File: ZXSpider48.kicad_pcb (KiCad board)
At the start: 2 copper layers, 213.5 x 130.5 mm, 152 parts, among them J1 Barrel_Jack_Switch, J11 EAR/MIC, J12 KB_CONN_05, J14 RESET, J15 ZX_48K_EDGE, J16 DB9_Pins, J17 ON/OFF, J18 JS_ENABLE, J19 AY3_IOB, J2 JTAG, J20 AY3_IOA, J3 9V, J4 AUDIO, J5 ROM_SW, J6 M-DIN KMDGX-9S-BS-1, J7 SPK_ON_OFF, J8 KB_CON_08, J9 UV/EEPROM, Q1 BC517, Q10 BC560, Q11 BC560, Q12 BC560, Q13 BC560, Q14 BC560, Q15 BC560, Q2 BC548, Q8 BC560, Q9 BC560, U1 AY-3-8912, U10 27/28C256, U11 74HCT240, U16 74LS138, U18 74LS00, U2 EPM7128SLC84-10, U3 LM7805_TO220, U4 AY-3-8910, U5 HM62256, U6 74HC04, U7 HM62256, U8 Z80, U9 74LS32, Y2 14.000 Mhz

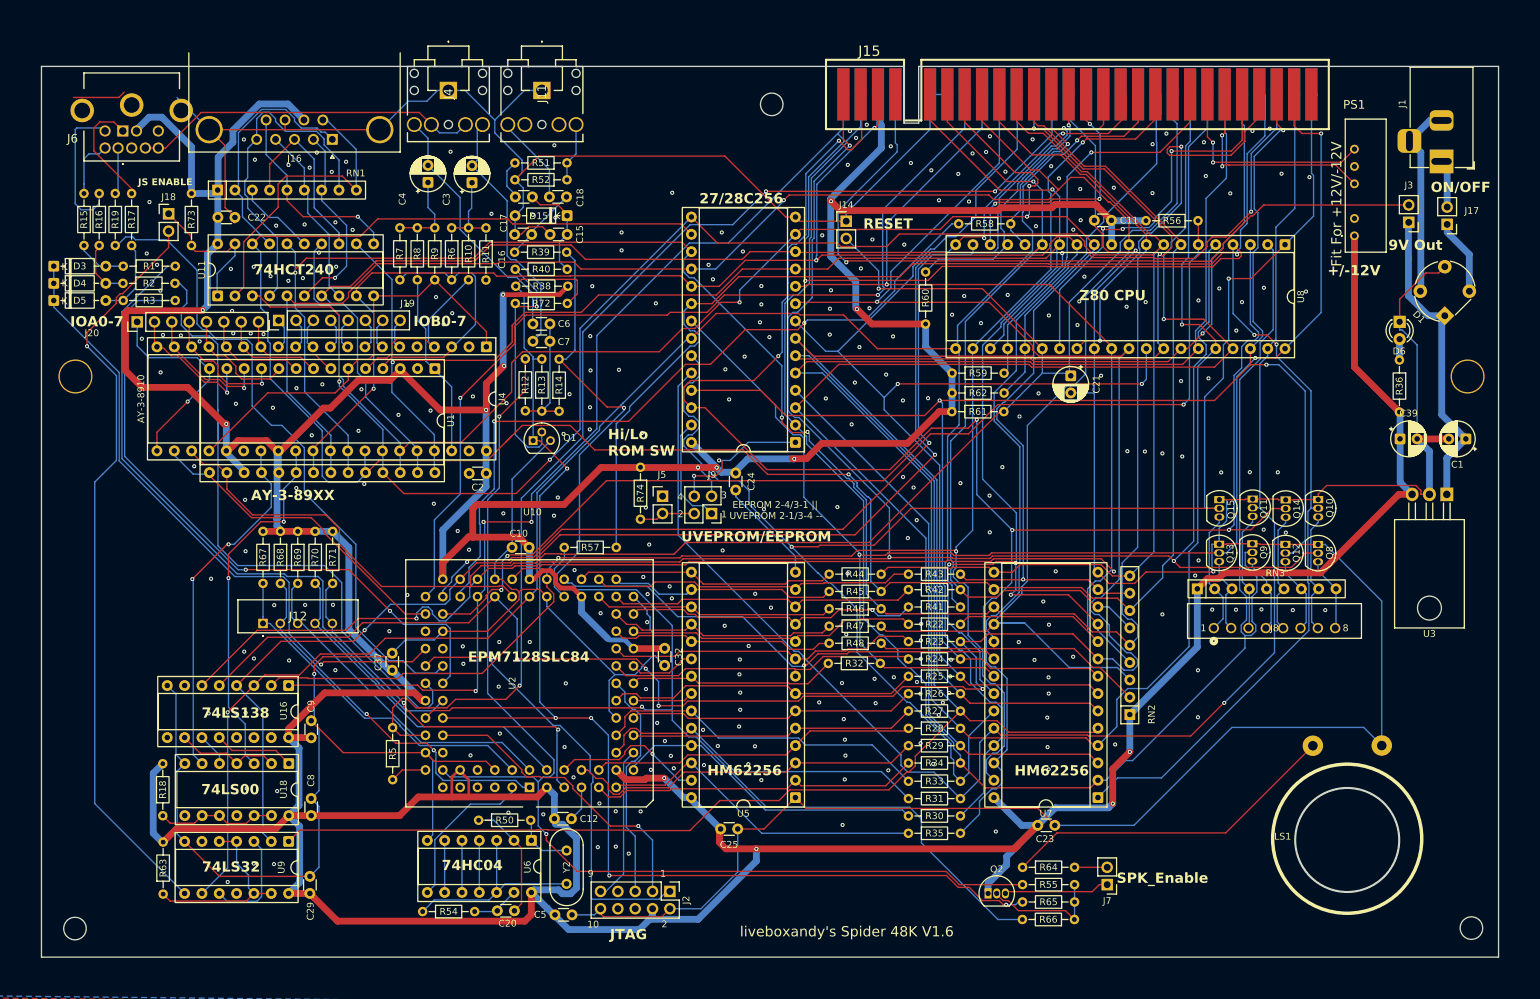
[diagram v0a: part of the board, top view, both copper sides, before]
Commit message: Add files via upload
Minor change to reduce PCB size to better fit some Rubber cases.
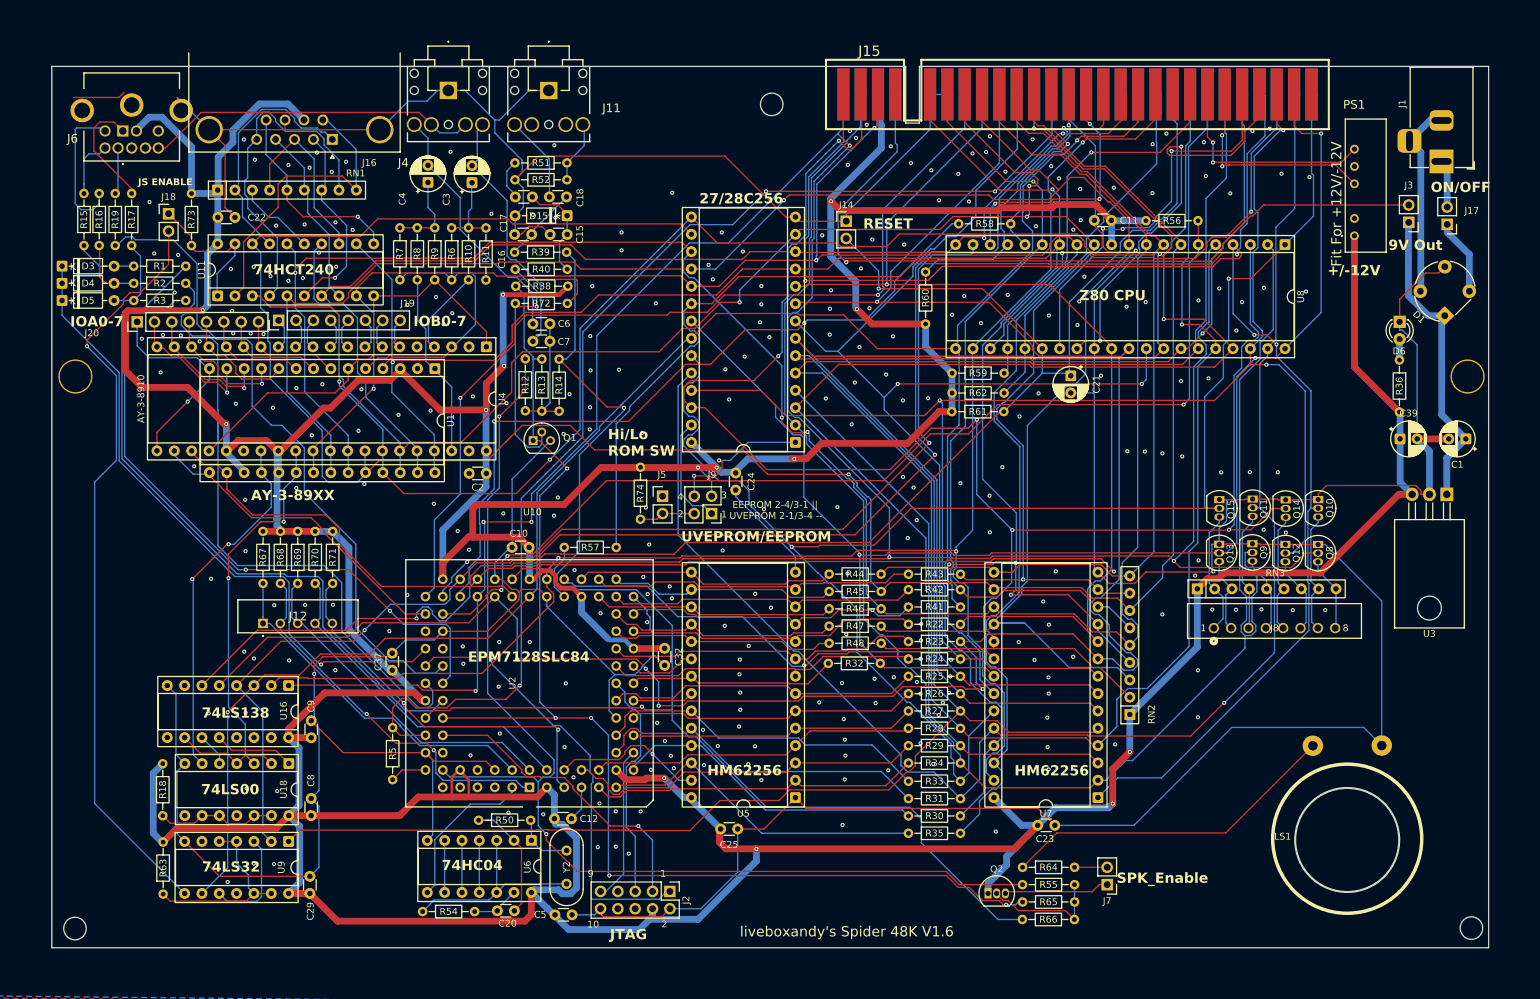
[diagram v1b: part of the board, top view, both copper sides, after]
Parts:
- moved R2 1.58 mm to (37.5, 53.7)
- moved R3 1.55 mm to (37.5, 56.2)
- moved R1 1.54 mm to (37.5, 51.1)
- moved D3 1.22 mm to (27.0, 51.1)
- moved D4 1.22 mm to (27.0, 53.7)
- moved D5 1.22 mm to (27.0, 56.2)
- moved J11 1.00 mm to (98.3, 25.4)
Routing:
- net GND: track 889.2 -> 890.7 mm
- net Net-(D3-A): track 7.36 -> 8.70 mm
- net RED: track 99.0 -> 100.3 mm
- net BLUE: track 95.7 -> 96.9 mm
- net Net-(J18-Pin_2): track 110.8 -> 111.4 mm
- net Net-(J11-Tip): track 13.1 -> 13.7 mm
- net CSYNC: track 96.4 -> 97.0 mm
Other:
- board size 213.5 x 130.5 mm -> 210.5 x 129.1 mm

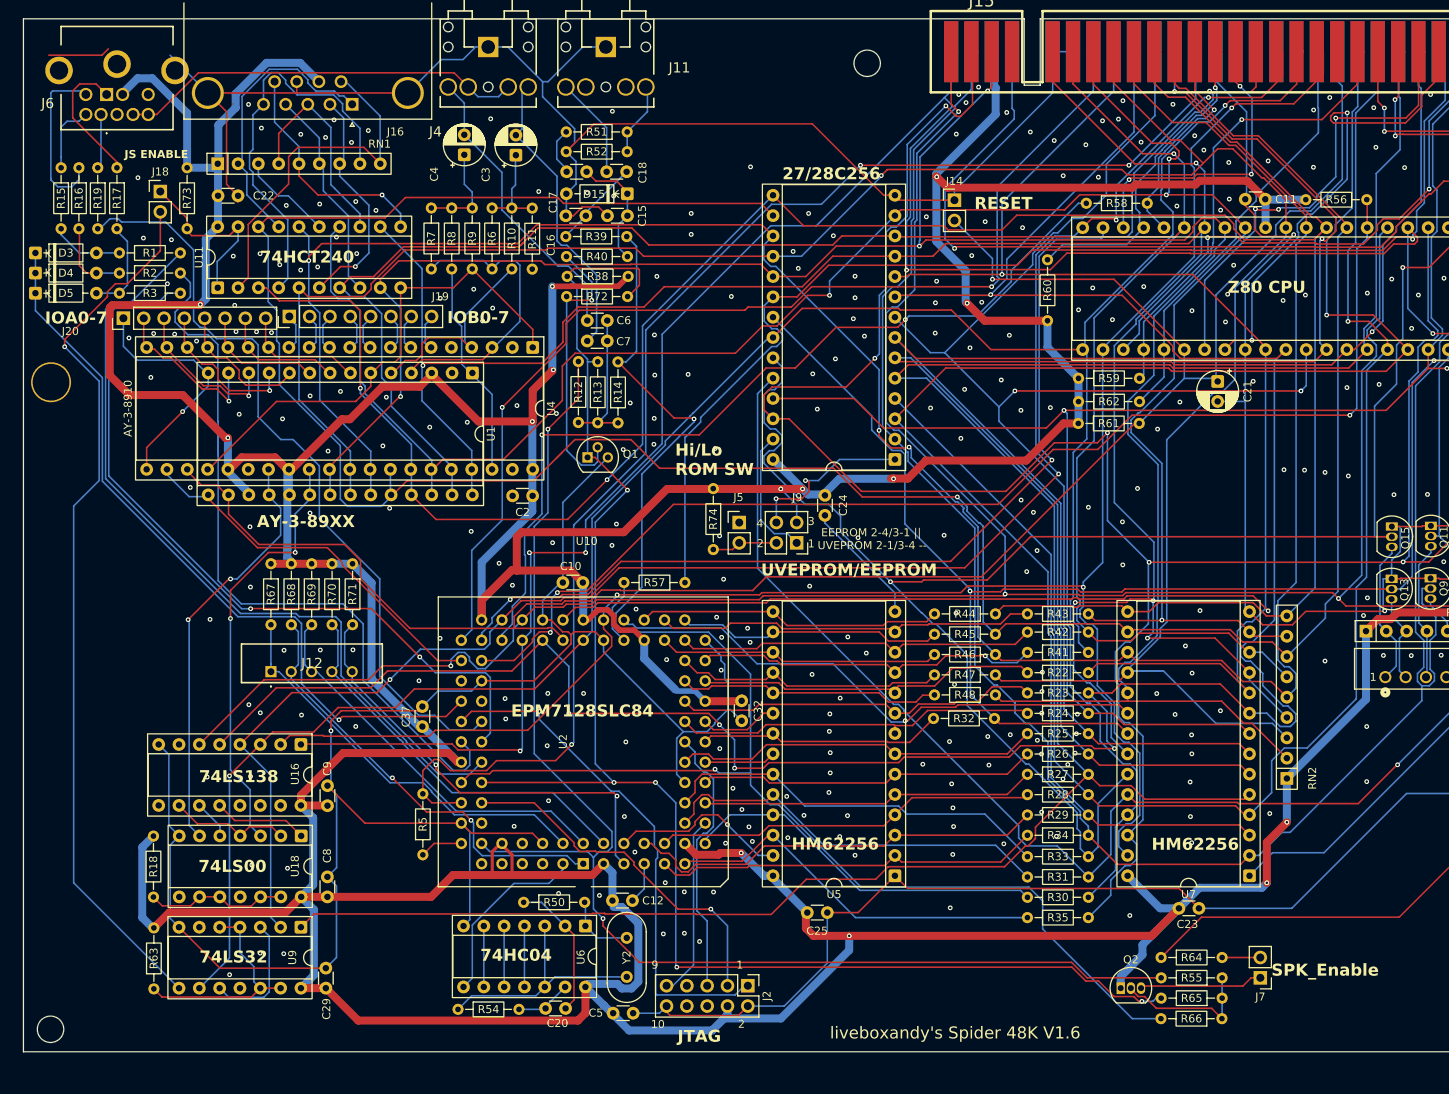
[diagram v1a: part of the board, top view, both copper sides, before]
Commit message: Add files via upload
Updated to V1,7 Added resistor for auto RGB switching. Added resistor/zener for auto AV switching. Updated README.MD
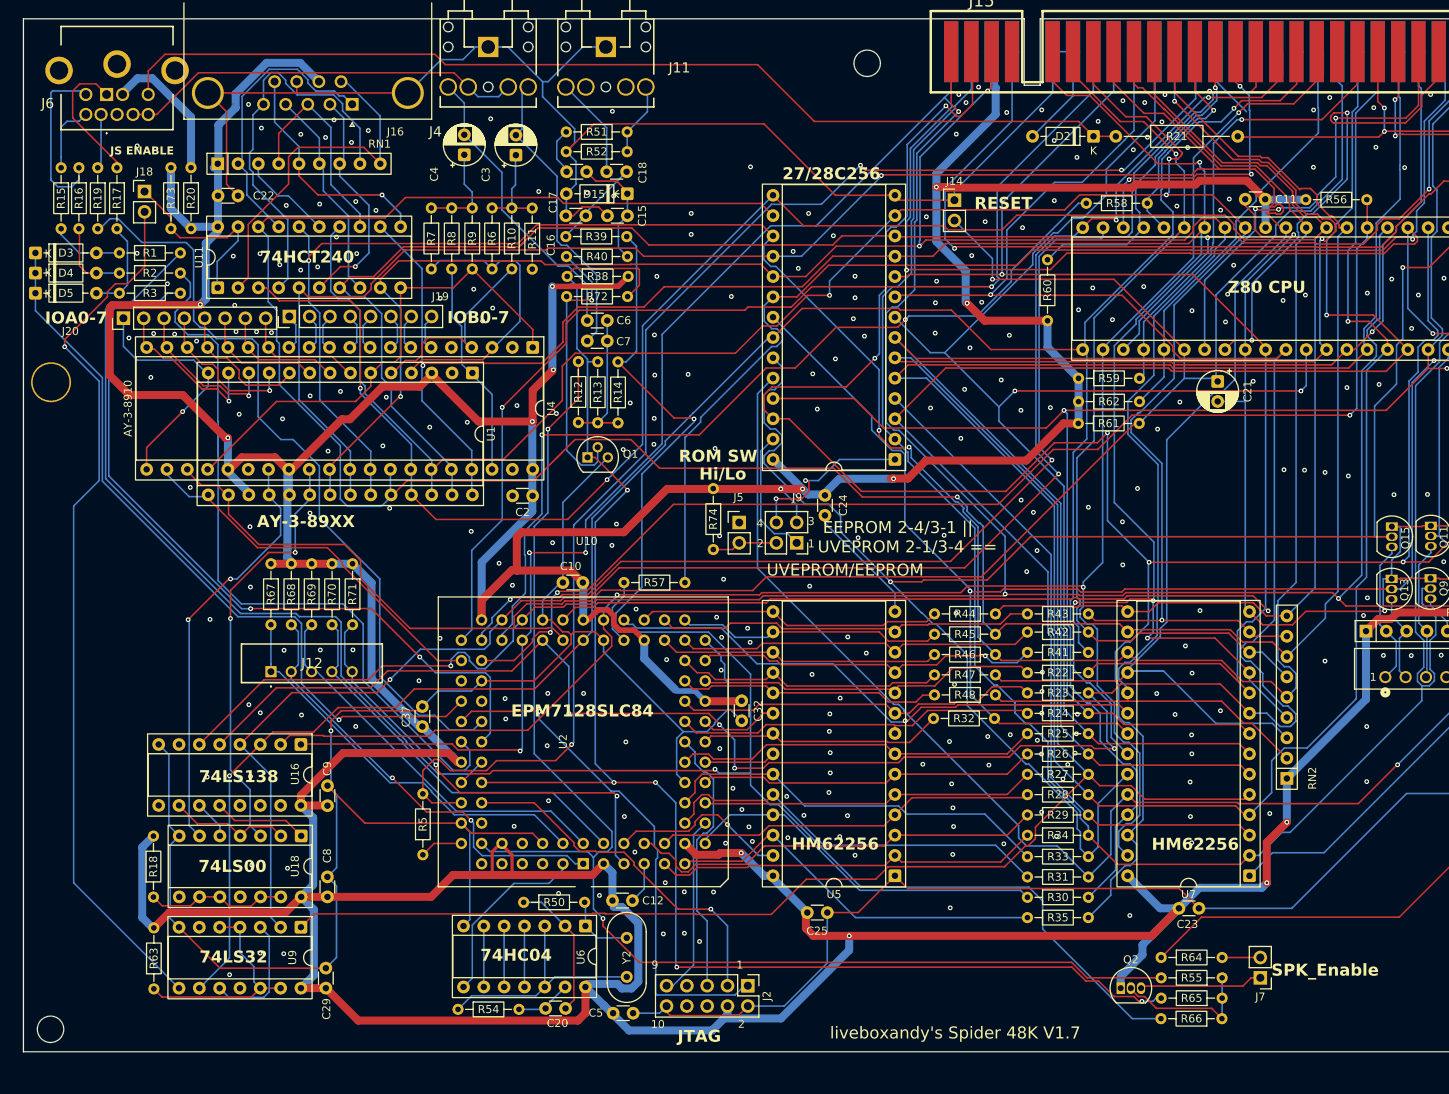
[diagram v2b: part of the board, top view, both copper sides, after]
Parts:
- added D2: 12V, Diode_THT:D_DO-35_SOD27_P7.62mm_Horizontal, F.Cu at (159.3, 36.6)
- added R20: 270R, Resistor_THT:R_Axial_DIN0204_L3.6mm_D1.6mm_P7.62mm_Horizontal, F.Cu at (46.5, 40.5)
- added R21: 150R, Resistor_THT:R_Axial_DIN0207_L6.3mm_D2.5mm_P15.24mm_Horizontal, F.Cu at (162.1, 36.6)
- moved R73 7.89 mm to (43.9, 40.5), turned to -90 degrees
- moved J18 1.97 mm to (40.6, 43.5)
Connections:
- J6 pad 10: GND -> unconnected-(J6-Pad10)
- J6 pad 11: GND -> unconnected-(J6-Pad11)
- J6 pad 12: GND -> unconnected-(J6-Pad12)
- J6 pad 2: +5V -> Net-(J6-Pad2)
- J6 pad 6: unconnected-(J6-Pad6) -> Net-(D2-K)
- R73 pad 1: Net-(J18-Pin_1) -> +5V
- R73 pad 2: +5V -> Net-(J18-Pin_1)
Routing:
- net Net-(D2-K): track 0.00 -> 129.0 mm
- net +12V: track 32.2 -> 50.8 mm
- net Net-(J6-Pad2): track 0.00 -> 17.8 mm
- net GND: track 890.7 -> 878.2 mm, vias 291 -> 288
- net +5V: track 986.6 -> 974.1 mm
- net D6: track 297.2 -> 301.7 mm
- net Net-(J18-Pin_1): track 22.7 -> 24.8 mm
- net A1: track 311.9 -> 314.0 mm
- net D3: track 308.1 -> 309.9 mm
- net D4: track 341.7 -> 343.2 mm
- net A3: track 186.9 -> 188.1 mm
- net WR: track 236.2 -> 235.1 mm
- net Net-(J18-Pin_2): track 111.4 -> 110.6 mm
- net D2: track 269.4 -> 270.0 mm
- net D1: track 259.4 -> 258.8 mm
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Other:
- board text added: "EEPROM 2-4/3-1 || UVEPROM 2-1/3-4 =="
- board text added: "liveboxandy's Spider 48K V1.7"
- board text removed: "EEPROM 2-4/3-1 || UVEPROM 2-1/3-4 --"
- board text removed: "liveboxandy's Spider 48K V1.6"
